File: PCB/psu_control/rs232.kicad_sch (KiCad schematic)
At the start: 7 parts, among them J16 RS232, U7 MAX3221E

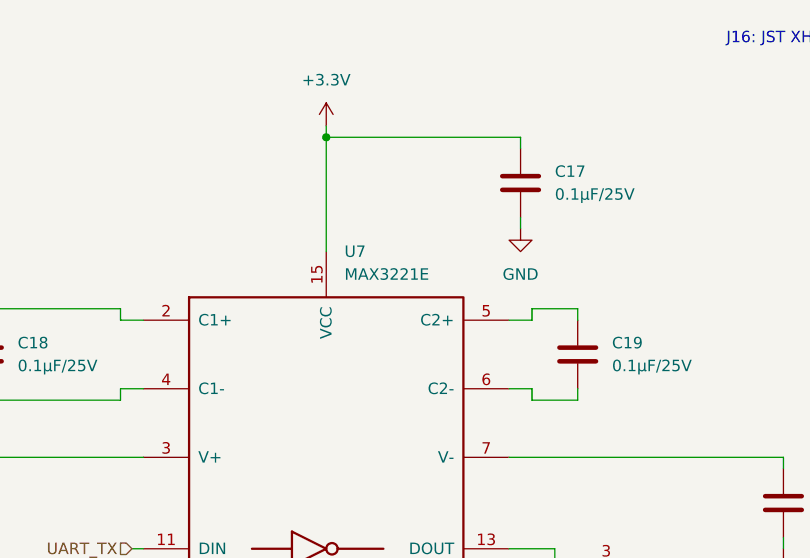
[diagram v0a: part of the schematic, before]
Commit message: Change MAX3221E by SN65C3221E.
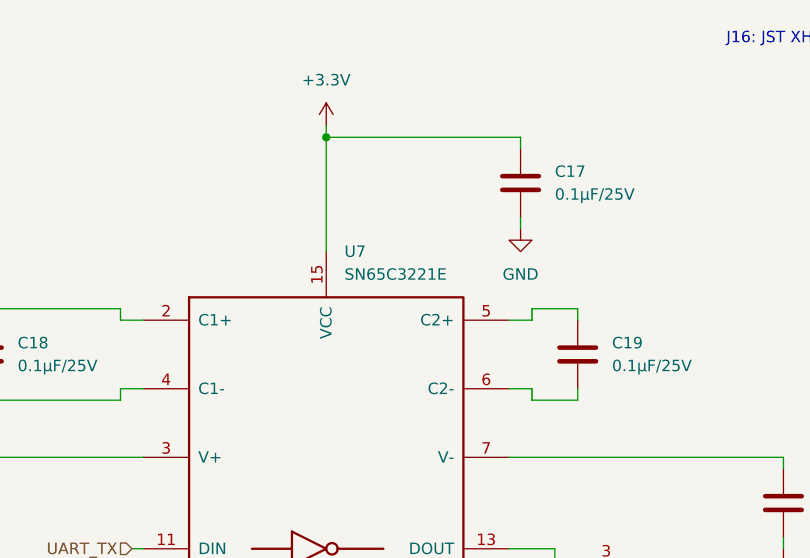
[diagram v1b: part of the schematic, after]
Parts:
- removed U7: MAX3221E, Package_SO:TSSOP-16_4.4x5mm_P0.65mm, symbol t-top:MAX3221E
- added U7: SN65C3221E, Package_SO:TSSOP-16_4.4x5mm_P0.65mm, symbol t-top:SN65C3221E
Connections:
- net +3.3V: now also U7.12 (FORCEON), U7.15 (VCC), U7.16 (~{FORCEOFF})
- net GND: now also U7.1 (~{EN}), U7.14 (GND)
- net UART_RX: now also U7.9 (ROUT)
- net UART_TX: now also U7.11 (DIN)
- net ~{INVALID}: now also U7.10 (~{INVALID})
- net at C18.1: now also U7.2 (C1+)
- net at C18.2: now also U7.4 (C1-)
- net at C20.1: now also U7.3 (V+)
- net at J16.3 (Pin_3): now also U7.13 (DOUT)
- net at C19.1: now also U7.5 (C2+)
- net at C19.2: now also U7.6 (C2-)
- net at C21.1: now also U7.7 (V-)
- net at J16.2 (Pin_2): now also U7.8 (RIN)
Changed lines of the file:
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@@
     (pin "1")
+  )
+  (symbol (lib_id "t-top:SN65C3221E") (at 77.47 68.58 0) (unit 1)
+    (in_bom yes) (on_board yes) (fields_autoplaced)
+    (property "Reference" "U7" (id 0) (at 79.4894 38.1 0)
+      (effects (font (size 1.27 1.27)) (justify left))
+    )
+    (property "Value" "SN65C3221E" (id 1) (at 79.4894 40.64 0)
+      (effects (font (size 1.27 1.27)) (justify left))
+    )
+    (property "Footprint" "Package_SO:TSSOP-16_4.4x5mm_P0.65mm" (id 2) (at 77.47 66.04 0)
+      (effects (font (size 1.27 1.27)) hide)
+    )
+    (property "Datasheet" "" (id 3) (at 77.47 66.04 0)
+      (effects (font (size 1.27 1.27)) hide)
+    )
+    (pin "1")
+    (pin "10")
+    (pin "11")
+    (pin "12")
+    (pin "13")
+    (pin "14")
+    (pin "15")
+    (pin "16")
+    (pin "2")
+    (pin "3")
+    (pin "4")
+    (pin "5")
+    (pin "6")
+    (pin "7")
+    (pin "8")
+    (pin "9")
   )
   (symbol (lib_id "Device:C") (at 39.37 49.53 0) (unit 1)
@@
     (pin "2")
   )
-  (symbol (lib_id "t-top:MAX3221E") (at 77.47 68.58 0) (unit 1)
-    (in_bom yes) (on_board yes) (fields_autoplaced)
-    (property "Reference" "U7" (id 0) (at 79.4894 38.1 0)
-      (effects (font (size 1.27 1.27)) (justify left))
-    )
-    (property "Value" "MAX3221E" (id 1) (at 79.4894 40.64 0)
-      (effects (font (size 1.27 1.27)) (justify left))
-    )
-    (property "Footprint" "Package_SO:TSSOP-16_4.4x5mm_P0.65mm" (id 2) (at 77.47 66.04 0)
-      (effects (font (size 1.27 1.27)) hide)
-    )
-    (property "Datasheet" "" (id 3) (at 77.47 66.04 0)
-      (effects (font (size 1.27 1.27)) hide)
-    )
-    (pin "1")
-    (pin "10")
-    (pin "11")
-    (pin "12")
-    (pin "13")
-    (pin "14")
-    (pin "15")
-    (pin "16")
-    (pin "2")
-    (pin "3")
-    (pin "4")
-    (pin "5")
-    (pin "6")
-    (pin "7")
-    (pin "8")
-    (pin "9")
-  )
   (symbol (lib_id "Device:C") (at 105.41 49.53 0) (unit 1)
